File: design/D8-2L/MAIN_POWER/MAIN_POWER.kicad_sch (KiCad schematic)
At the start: 15 parts, among them J1 12V INPUT - FLAT SOLDER PADS, J2 JETSON 12V 5A, J3 GMSL 12V / EXCLUSIVE WITH POE, J4 FAN 12V 0.14A, J5 USB BOARD 12V, J6 POE BOARD 12V INPUT

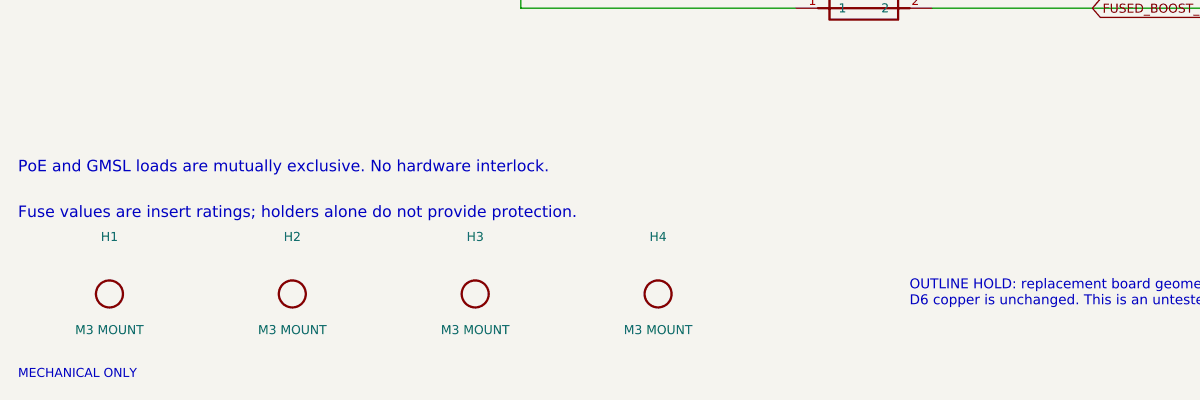
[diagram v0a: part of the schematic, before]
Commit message: Apply MAIN V3 outline and export FASTON STEP
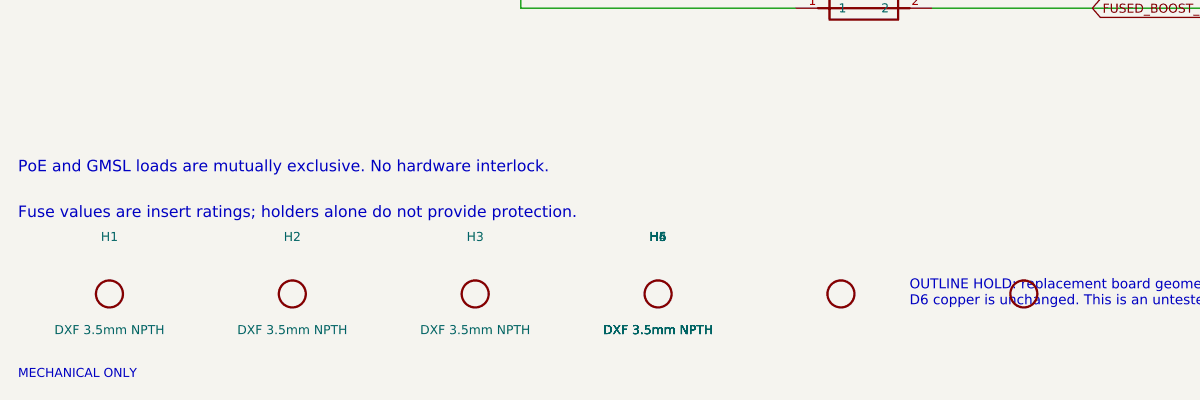
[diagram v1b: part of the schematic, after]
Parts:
- added H5, H6: DXF 3.5mm NPTH, UMI_D2:MountingHole_3.5mm, symbol UMI:P_H4
- H1, H2, H3, H4: value M3 MOUNT -> DXF 3.5mm NPTH; footprint UMI_D2:MountingHole_4.5mm -> UMI_D2:MountingHole_3.5mm
